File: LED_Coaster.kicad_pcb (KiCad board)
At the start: 2 copper layers, 90 x 90 mm, 45 parts, among them J1 USB_C_Receptacle_USB2.0, SW1 SW_Push, U1 ATmega32U4-A, Y1 Crystal_GND24

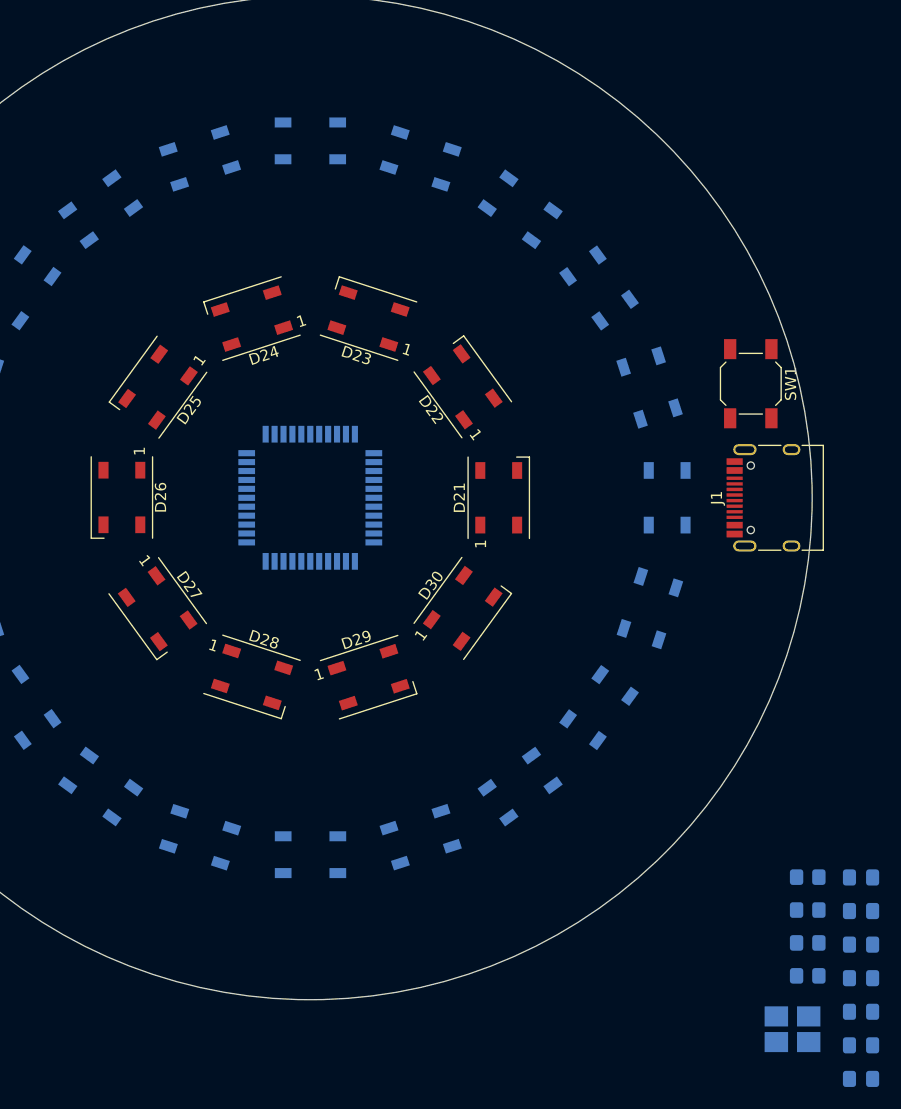
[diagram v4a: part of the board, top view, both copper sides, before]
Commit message: Placed all components
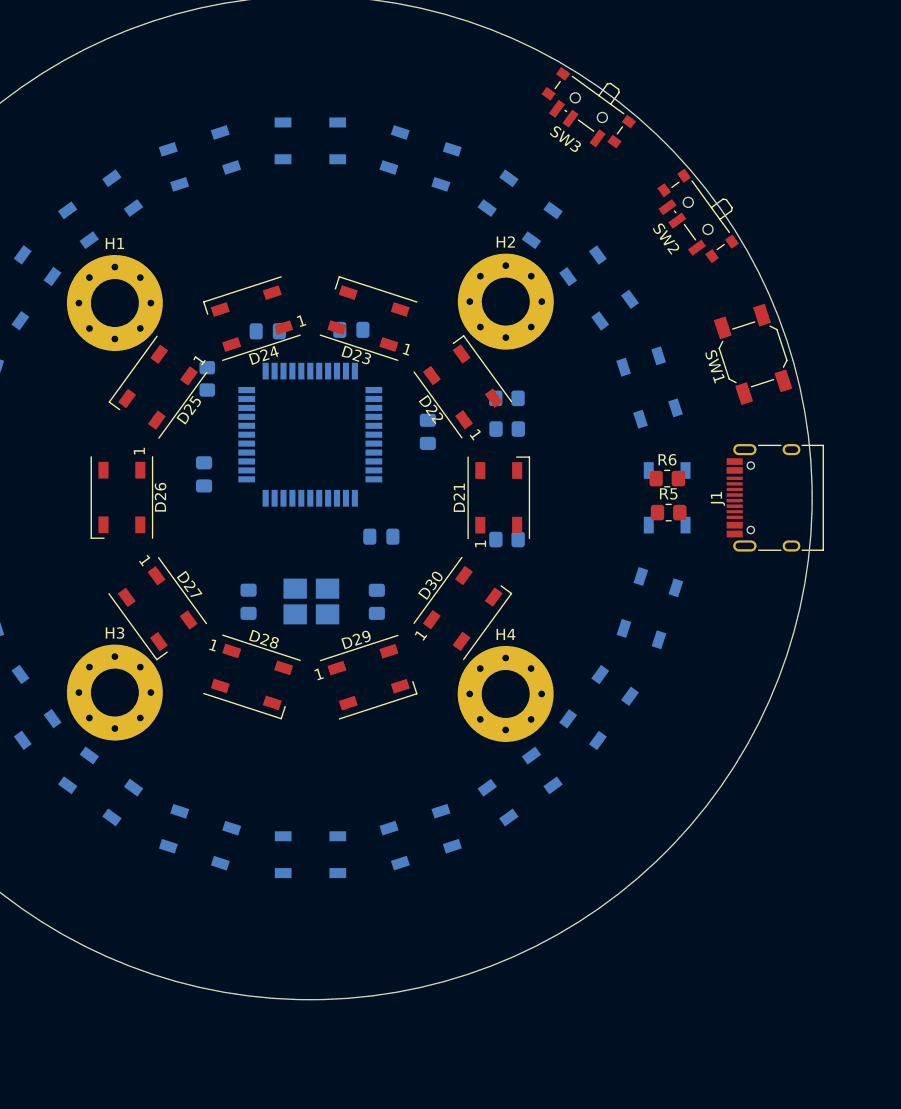
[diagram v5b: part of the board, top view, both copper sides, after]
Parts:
- added H1: MountingHole, MountingHole:MountingHole_4.3mm_M4_Pad_Via, F.Cu at (132.5, 62.5)
- added H2: MountingHole, MountingHole:MountingHole_4.3mm_M4_Pad_Via, F.Cu at (167.5, 62.4)
- added H3: MountingHole, MountingHole:MountingHole_4.3mm_M4_Pad_Via, F.Cu at (132.5, 97.5)
- added H4: MountingHole, MountingHole:MountingHole_4.3mm_M4_Pad_Via, F.Cu at (167.5, 97.6)
- added R5: 5.1K, Resistor_SMD:R_0805_2012Metric_Pad1.20x1.40mm_HandSolder, F.Cu at (182.1, 81.3)
- added R6: 5.1K, Resistor_SMD:R_0805_2012Metric_Pad1.20x1.40mm_HandSolder, F.Cu at (182.0, 78.3)
- added SW2: SW_DIP_x01, Button_Switch_SMD:SW_SPDT_PCM12, F.Cu at (184.5, 54.9)
- added SW3: SW_DIP_x01, Button_Switch_SMD:SW_SPDT_PCM12, F.Cu at (174.8, 45.3)
- moved C3 76.5 mm to (146.2, 65.1), turned to 0 degrees
- moved C5 76.1 mm to (140.5, 77.9), turned to -90 degrees
- moved R1 70.0 mm to (140.8, 69.3), turned to 90 degrees
- moved C2 69.3 mm to (153.7, 64.9)
- moved C6 67.8 mm to (144.5, 89.3), turned to 90 degrees
- moved C7 60.9 mm to (156.0, 89.3), turned to -90 degrees
- moved C4 58.5 mm to (156.4, 83.5)
- moved Y1 57.7 mm to (150.1, 89.3), turned to 0 degrees
- moved R3 55.8 mm to (167.6, 71.1)
- moved C1 55.7 mm to (160.5, 74.1), turned to 90 degrees
- moved R2 50.9 mm to (167.7, 73.8)
- moved R4 47.5 mm to (167.6, 83.7), turned to 0 degrees
- moved U1 5.66 mm to (150.0, 74.3)
- moved SW1 2.64 mm to (189.7, 67.1), turned to 108 degrees
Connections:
- D1 pad 1: +5V -> Net-(D1-VDD)
- D10 pad 1: +5V -> Net-(D1-VDD)
- D11 pad 1: +5V -> Net-(D1-VDD)
- D12 pad 1: +5V -> Net-(D1-VDD)
- D13 pad 1: +5V -> Net-(D1-VDD)
- D14 pad 1: +5V -> Net-(D1-VDD)
- D15 pad 1: +5V -> Net-(D1-VDD)
- D16 pad 1: +5V -> Net-(D1-VDD)
- D17 pad 1: +5V -> Net-(D1-VDD)
- D18 pad 1: +5V -> Net-(D1-VDD)
- D19 pad 1: +5V -> Net-(D1-VDD)
- D2 pad 1: +5V -> Net-(D1-VDD)
- D20 pad 1: +5V -> Net-(D1-VDD)
- D21 pad 1: +5V -> Net-(D21-VDD)
- D22 pad 1: +5V -> Net-(D21-VDD)
- D23 pad 1: +5V -> Net-(D21-VDD)
- D24 pad 1: +5V -> Net-(D21-VDD)
- D25 pad 1: +5V -> Net-(D21-VDD)
- D26 pad 1: +5V -> Net-(D21-VDD)
- D27 pad 1: +5V -> Net-(D21-VDD)
- D28 pad 1: +5V -> Net-(D21-VDD)
- D29 pad 1: +5V -> Net-(D21-VDD)
- D3 pad 1: +5V -> Net-(D1-VDD)
- D30 pad 1: +5V -> Net-(D21-VDD)
- D4 pad 1: +5V -> Net-(D1-VDD)
- D5 pad 1: +5V -> Net-(D1-VDD)
- D6 pad 1: +5V -> Net-(D1-VDD)
- D7 pad 1: +5V -> Net-(D1-VDD)
- D8 pad 1: +5V -> Net-(D1-VDD)
- D9 pad 1: +5V -> Net-(D1-VDD)
- J1 pad A1: Net-(J1-GND-PadA1) -> GND
- J1 pad A12: Net-(J1-GND-PadA1) -> GND
- J1 pad A4: Net-(J1-VBUS-PadA4) -> +5V
- J1 pad A5: unconnected-(J1-CC1-PadA5) -> Net-(J1-CC1)
- J1 pad A6: unconnected-(J1-D+-PadA6) -> /D+
- J1 pad A7: unconnected-(J1-D--PadA7) -> /D-
- J1 pad A9: Net-(J1-VBUS-PadA4) -> +5V
- J1 pad B1: Net-(J1-GND-PadA1) -> GND
- J1 pad B12: Net-(J1-GND-PadA1) -> GND
- J1 pad B4: Net-(J1-VBUS-PadA4) -> +5V
- J1 pad B5: unconnected-(J1-CC2-PadB5) -> Net-(J1-CC2)
- J1 pad B6: unconnected-(J1-D+-PadB6) -> /D+
- J1 pad B7: unconnected-(J1-D--PadB7) -> /D-
- J1 pad B9: Net-(J1-VBUS-PadA4) -> +5V
- J1 pad S1: unconnected-(J1-SHIELD-PadS1) -> GND

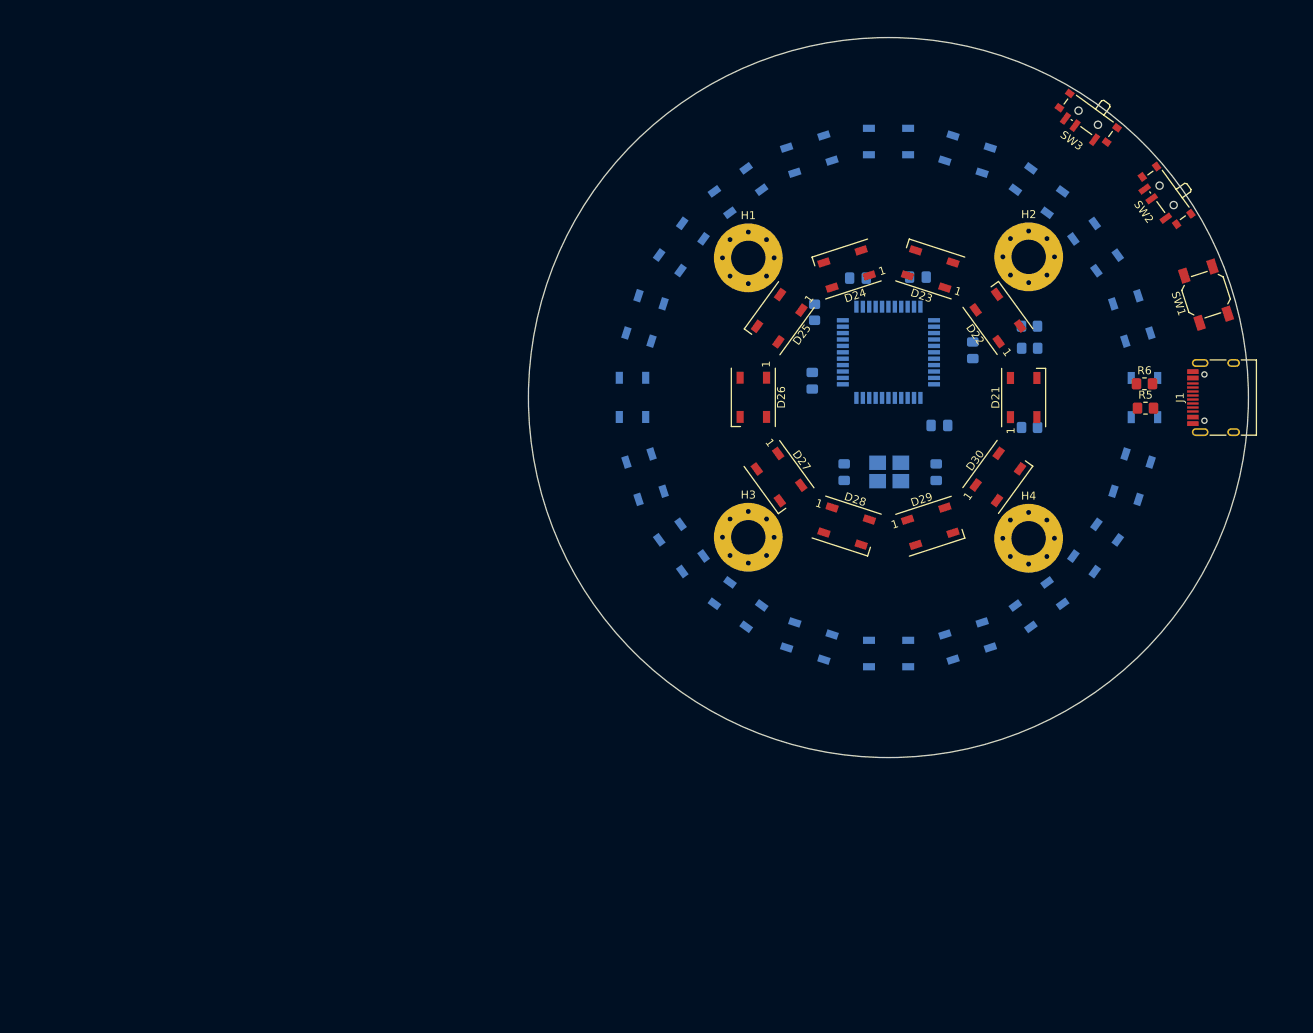
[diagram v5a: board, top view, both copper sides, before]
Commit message: Added traces and datasheets
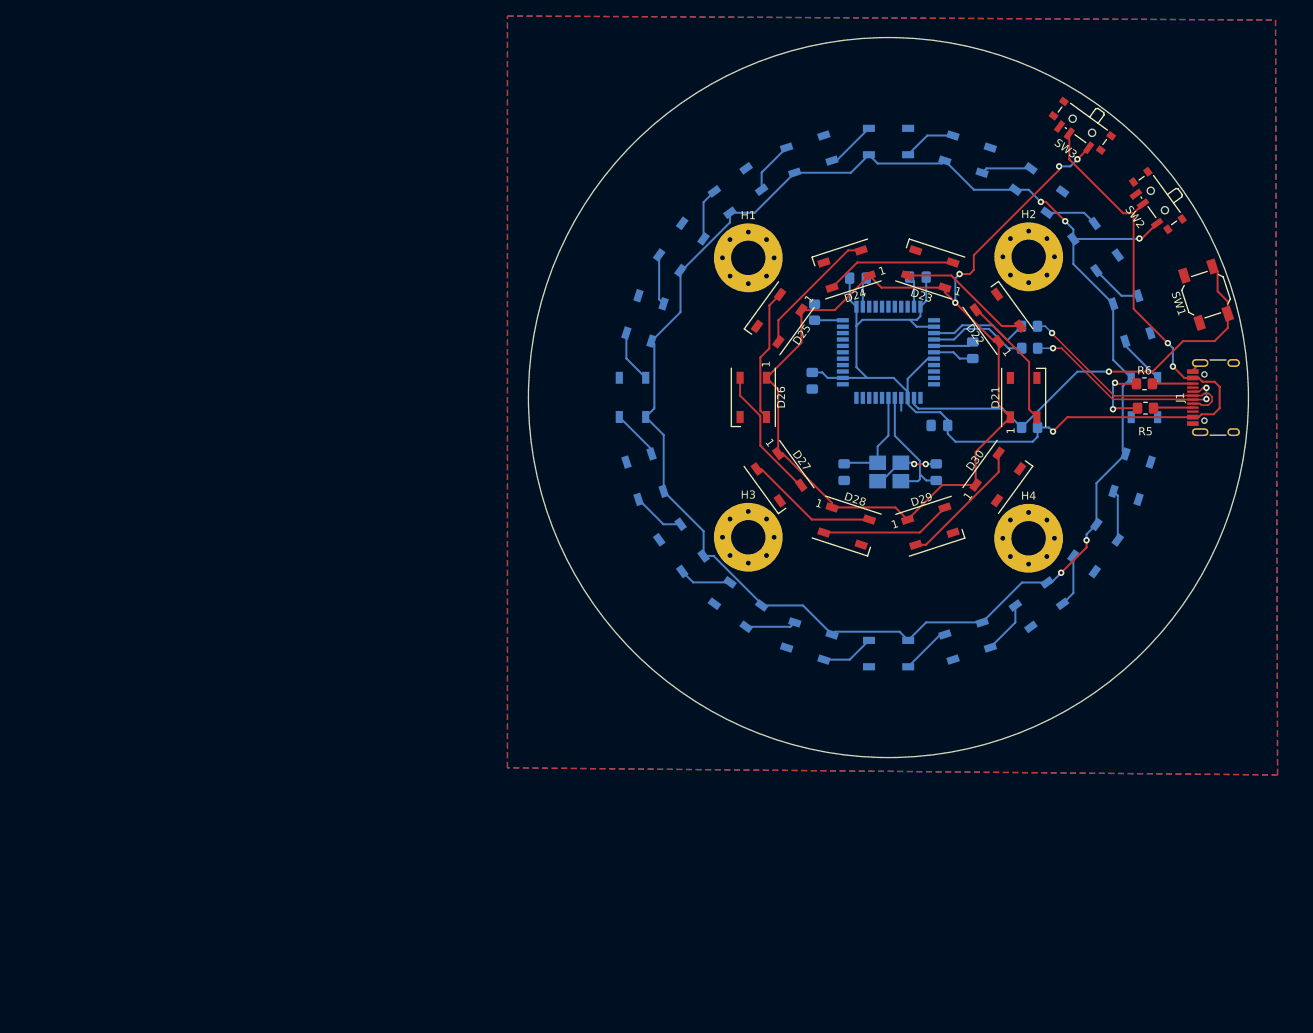
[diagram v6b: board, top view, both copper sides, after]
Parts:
- moved SW2 1.27 mm to (183.4, 55.6)
- moved SW3 1.24 mm to (174.0, 46.3)
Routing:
- net Net-(D1-VDD): track 0.00 -> 215.2 mm, vias 0 -> 5
- net +5V: track 0.00 -> 142.9 mm, vias 0 -> 3
- net Net-(D21-VDD): track 0.00 -> 129.3 mm, vias 0 -> 4
- net Net-(U1-~{RESET}): track 0.00 -> 55.0 mm, vias 0 -> 1
- net GND: track 0.00 -> 34.3 mm, vias 0 -> 4
- net /D-: track 0.00 -> 29.0 mm, vias 0 -> 1
- net /D+: track 0.00 -> 27.1 mm, vias 0 -> 3
- net Net-(D26-DOUT): track 0.00 -> 16.7 mm
- net Net-(D22-DOUT): track 0.00 -> 16.7 mm
- net Net-(D27-DOUT): track 0.00 -> 16.7 mm
- net Net-(D21-DOUT): track 0.00 -> 16.7 mm
- net Net-(D24-DOUT): track 0.00 -> 16.7 mm
- net Net-(D25-DOUT): track 0.00 -> 16.6 mm
- net Net-(D29-DOUT): track 0.00 -> 16.5 mm
- net Net-(D23-DOUT): track 0.00 -> 16.4 mm
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- added copper zone on B.Cu, net GND
- added copper zone on F.Cu, net GND

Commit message: Added a fuse
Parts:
- added D31: LED, LED_SMD:LED_0805_2012Metric_Pad1.15x1.40mm_HandSolder, F.Cu at (187.0, 61.0)
- added D32: LED, LED_SMD:LED_0805_2012Metric_Pad1.15x1.40mm_HandSolder, F.Cu at (179.1, 50.1)
- added D33: LED, LED_SMD:LED_0805_2012Metric_Pad1.15x1.40mm_HandSolder, F.Cu at (191.0, 88.3)
- added F1: Polyfuse, Fuse:Fuse_1206_3216Metric_Pad1.42x1.75mm_HandSolder, F.Cu at (182.1, 85.0)
- added R7: 150, Resistor_SMD:R_0805_2012Metric_Pad1.20x1.40mm_HandSolder, F.Cu at (182.9, 62.7)
- added R8: 150, Resistor_SMD:R_0805_2012Metric_Pad1.20x1.40mm_HandSolder, F.Cu at (175.3, 52.9)
- added R9: 150, Resistor_SMD:R_0805_2012Metric_Pad1.20x1.40mm_HandSolder, F.Cu at (182.2, 88.3)
- turned H1 to 90 degrees
- turned H2 to 90 degrees
- turned H3 to 90 degrees
- turned H4 to 90 degrees
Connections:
- J1 pad A4: +5V -> Net-(F1-Pad2)
- J1 pad A9: +5V -> Net-(F1-Pad2)
- J1 pad B4: +5V -> Net-(F1-Pad2)
- J1 pad B9: +5V -> Net-(F1-Pad2)
- U1 pad 10: unconnected-(U1-PB2-Pad10) -> /large_ring
- U1 pad 8: unconnected-(U1-PB0-Pad8) -> Net-(U1-PB0)
- U1 pad 9: unconnected-(U1-PB1-Pad9) -> /small_ring
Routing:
- net Net-(U1-PB0): track 0.00 -> 33.2 mm, vias 0 -> 3
- net /large_ring: track 0.00 -> 30.8 mm, vias 0 -> 2
- net Net-(F1-Pad2): track 0.00 -> 15.8 mm
- net /small_ring: track 0.00 -> 11.9 mm, vias 0 -> 1
- net +5V: track 142.9 -> 135.2 mm, vias 3 -> 4
- net Net-(D33-A): track 0.00 -> 6.74 mm
- net Net-(D32-A): track 0.00 -> 3.55 mm
- net GND: track 34.3 -> 37.8 mm, vias 4 -> 5
- net Net-(D31-A): track 0.00 -> 3.40 mm
- net Net-(D1-VDD): track 215.2 -> 218.3 mm
- net Net-(D21-VDD): track 129.3 -> 131.7 mm

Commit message: Version 1 done
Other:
- board text added: "Inner"
- board text added: "Outer"
- board text added: "{dblquote}Important gaps remain{dblquote}"
